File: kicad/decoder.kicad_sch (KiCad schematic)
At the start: 6 parts, among them U2 28C64, U3 28C64, U4 28C64

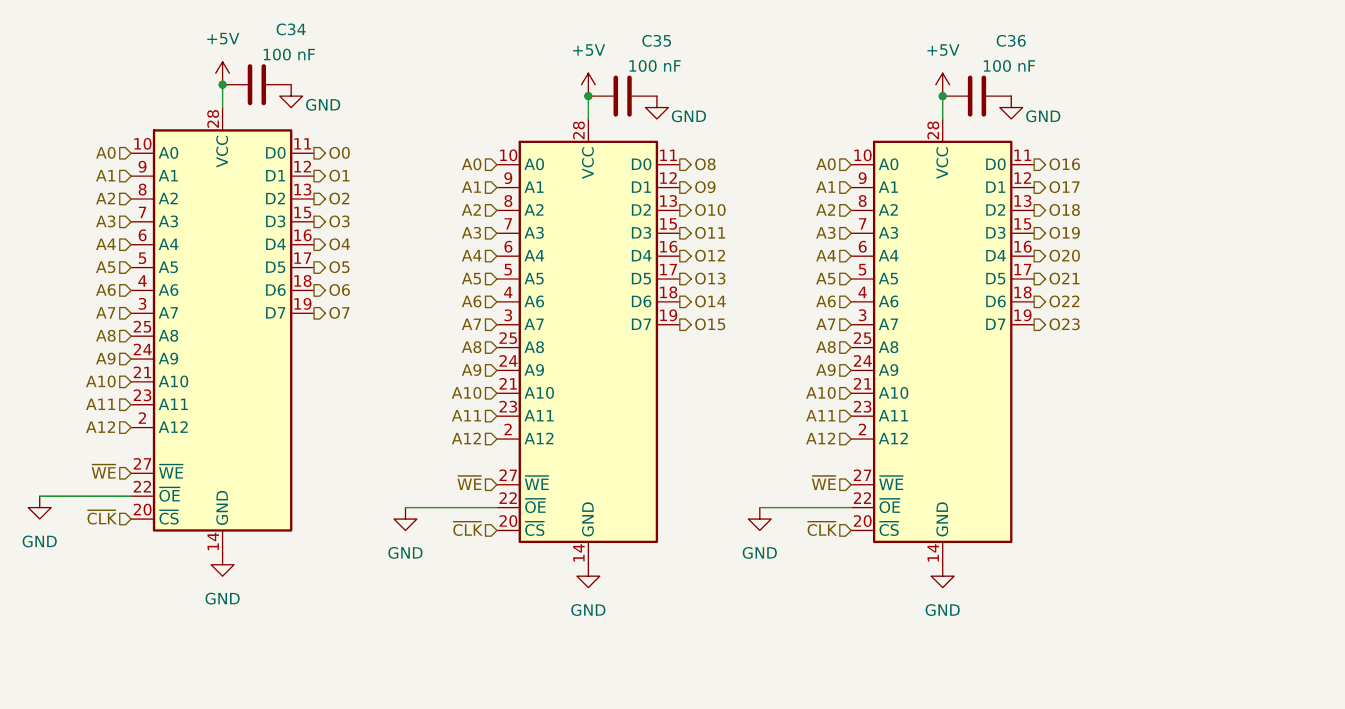
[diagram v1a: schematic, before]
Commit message: kicad: compact design
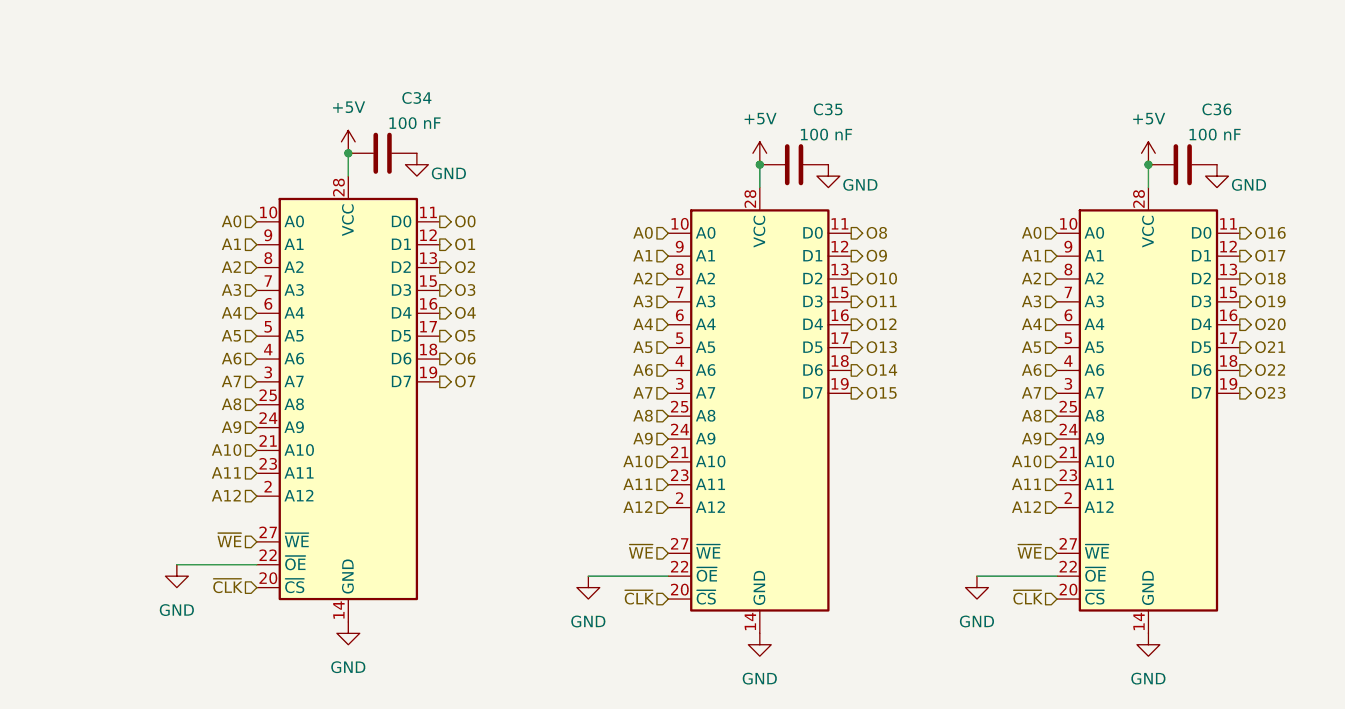
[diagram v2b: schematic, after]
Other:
- moved on the sheet: C34, C35, C36

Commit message: kicad: finalize sketch
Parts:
- DECODER_U0: renamed from U2; footprint (none) -> Package_DIP:DIP-28_W15.24mm
- DECODER_U0_C1: renamed from C34; footprint (none) -> Capacitor_THT:C_Disc_D3.0mm_W1.6mm_P2.50mm
- DECODER_U1: renamed from U3; footprint (none) -> Package_DIP:DIP-28_W15.24mm
- DECODER_U1_C1: renamed from C35; footprint (none) -> Capacitor_THT:C_Disc_D3.0mm_W1.6mm_P2.50mm
- DECODER_U2: renamed from U4; footprint (none) -> Package_DIP:DIP-28_W15.24mm
- DECODER_U2_C1: renamed from C36; footprint (none) -> Capacitor_THT:C_Disc_D3.0mm_W1.6mm_P2.50mm
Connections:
- removed net ~{WE}: DECODER_U0.27 (~{WE}), DECODER_U1.27 (~{WE}), DECODER_U2.27 (~{WE})
- no-connect marks 0 -> 3
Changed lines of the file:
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@@
 		(color 0 0 0 0)
+	)
+	(no_connect
+		(at 139.7 76.2)
+	)
+	(no_connect
+		(at 96.52 76.2)
+	)
+	(no_connect
+		(at 50.8 74.93)
 	)
 	(wire
@@
 		)
 	)
-	(hierarchical_label "~{WE}"
-		(shape input)
-		(at 50.8 74.93 180)
-		(effects
-			(font
-				(size 1.27 1.27)
-			)
-			(justify right)
-		)
-	)
 	(hierarchical_label "A5"
 		(shape input)
@@
 		)
 	)
-	(hierarchical_label "~{WE}"
-		(shape input)
-		(at 139.7 76.2 180)
-		(effects
-			(font
-				(size 1.27 1.27)
-			)
-			(justify right)
-		)
-	)
 	(hierarchical_label "A3"
 		(shape input)
@@
 		(shape input)
 		(at 139.7 68.58 180)
-		(effects
-			(font
-				(size 1.27 1.27)
-			)
-			(justify right)
-		)
-	)
-	(hierarchical_label "~{WE}"
-		(shape input)
-		(at 96.52 76.2 180)
 		(effects
 			(font
@@
 		(on_board yes)
 		(dnp no)
-		(property "Reference" "C34"
-			(at 68.58 25.654 90)
+		(property "Reference" "DECODER_U0_C1"
+			(at 72.136 26.67 90)
 			(effects
 				(font
@@
 			)
 		)
-		(property "Footprint" ""
+		(property "Footprint" "Capacitor_THT:C_Disc_D3.0mm_W1.6mm_P2.50mm"
 			(at 68.58 30.7848 0)
 			(effects
@@
 			(project "SC08v2"
 				(path "/8273a279-6d4f-43cc-a94b-c590a7d8a356/b5d1b334-e53f-4677-aa25-7c0c18a7a6bc"
-					(reference "C34")
+					(reference "DECODER_U0_C1")
 					(unit 1)
 				)
@@
 		(on_board yes)
 		(dnp no)
-		(property "Reference" "C36"
-			(at 157.48 26.924 90)
+		(property "Reference" "DECODER_U2_C1"
+			(at 160.782 27.94 90)
 			(effects
 				(font
@@
 			)
 		)
-		(property "Footprint" ""
+		(property "Footprint" "Capacitor_THT:C_Disc_D3.0mm_W1.6mm_P2.50mm"
 			(at 157.48 32.0548 0)
 			(effects
@@
 			(project "SC08v2"
 				(path "/8273a279-6d4f-43cc-a94b-c590a7d8a356/b5d1b334-e53f-4677-aa25-7c0c18a7a6bc"
-					(reference "C36")
+					(reference "DECODER_U2_C1")
 					(unit 1)
 				)
@@
 	)
 	(symbol
+		(lib_name "28C64_1")
 		(lib_id "custom:28C64")
 		(at 60.96 58.42 0)
@@
 		(on_board yes)
 		(dnp no)
-		(fields_autoplaced yes)
-		(property "Reference" "U2"
-			(at 59.944 46.482 0)
-			(effects
-				(font
-					(size 1.27 1.27)
-				)
-				(hide yes)
+		(property "Reference" "DECODER_U0"
+			(at 71.12 83.312 0)
+			(effects
+				(font
+					(size 1.27 1.27)
+				)
 			)
 		)
 		(property "Value" "28C64"
-			(at 57.912 60.198 0)
+			(at 65.786 85.09 0)
 			(effects
 				(font
@@
 				)
 				(justify left)
-				(hide yes)
-			)
-		)
-		(property "Footprint" ""
+			)
+		)
+		(property "Footprint" "Package_DIP:DIP-28_W15.24mm"
 			(at 60.96 58.42 0)
 			(effects
@@
 		)
 		(pin "11"
+		)
+		(pin "1"
+		)
+		(pin "26"
 		)
 		(instances
 			(project "SC08v2"
 				(path "/8273a279-6d4f-43cc-a94b-c590a7d8a356/b5d1b334-e53f-4677-aa25-7c0c18a7a6bc"
-					(reference "U2")
+					(reference "DECODER_U0")
 					(unit 1)
 				)
@@
 		(on_board yes)
 		(dnp no)
-		(property "Reference" "C35"
-			(at 114.3 26.924 90)
+		(property "Reference" "DECODER_U1_C1"
+			(at 117.856 27.686 90)
 			(effects
 				(font
@@
 			)
 		)
-		(property "Footprint" ""
+		(property "Footprint" "Capacitor_THT:C_Disc_D3.0mm_W1.6mm_P2.50mm"
 			(at 114.3 32.0548 0)
 			(effects
@@
 			(project "SC08v2"
 				(path "/8273a279-6d4f-43cc-a94b-c590a7d8a356/b5d1b334-e53f-4677-aa25-7c0c18a7a6bc"
-					(reference "C35")
+					(reference "DECODER_U1_C1")
 					(unit 1)
 				)
@@
 		(on_board yes)
 		(dnp no)
-		(fields_autoplaced yes)
-		(property "Reference" "U4"
-			(at 148.844 47.752 0)
-			(effects
-				(font
-					(size 1.27 1.27)
-				)
-				(hide yes)
+		(property "Reference" "DECODER_U2"
+			(at 160.274 84.836 0)
+			(effects
+				(font
+					(size 1.27 1.27)
+				)
 			)
 		)
 		(property "Value" "28C64"
-			(at 146.812 61.468 0)
+			(at 155.448 86.614 0)
 			(effects
 				(font
@@
 				)
 				(justify left)
-				(hide yes)
-			)
-		)
-		(property "Footprint" ""
+			)
+		)
+		(property "Footprint" "Package_DIP:DIP-28_W15.24mm"
 			(at 149.86 59.69 0)
 			(effects
@@
 		)
 		(pin "11"
+		)
+		(pin "26"
+		)
+		(pin "1"
 		)
 		(instances
 			(project "SC08v2"
 				(path "/8273a279-6d4f-43cc-a94b-c590a7d8a356/b5d1b334-e53f-4677-aa25-7c0c18a7a6bc"
-					(reference "U4")
+					(reference "DECODER_U2")
 					(unit 1)
 				)
@@
 	)
 	(symbol
+		(lib_name "28C64_2")
 		(lib_id "custom:28C64")
 		(at 106.68 59.69 0)
@@
 		(on_board yes)
 		(dnp no)
-		(fields_autoplaced yes)
-		(property "Reference" "U3"
-			(at 105.664 47.752 0)
-			(effects
-				(font
-					(size 1.27 1.27)
-				)
-				(hide yes)
+		(property "Reference" "DECODER_U1"
+			(at 116.078 84.582 0)
+			(effects
+				(font
+					(size 1.27 1.27)
+				)
 			)
 		)
 		(property "Value" "28C64"
-			(at 103.632 61.468 0)
+			(at 111.252 87.122 0)
 			(effects
 				(font
@@
 				)
 				(justify left)
-				(hide yes)
-			)
-		)
-		(property "Footprint" ""
+			)
+		)
+		(property "Footprint" "Package_DIP:DIP-28_W15.24mm"
 			(at 106.68 59.69 0)
 			(effects
@@
 		)
 		(pin "11"
+		)
+		(pin "1"
+		)
+		(pin "26"
 		)
 		(instances
 			(project "SC08v2"
 				(path "/8273a279-6d4f-43cc-a94b-c590a7d8a356/b5d1b334-e53f-4677-aa25-7c0c18a7a6bc"
-					(reference "U3")
+					(reference "DECODER_U1")
 					(unit 1)
 				)
